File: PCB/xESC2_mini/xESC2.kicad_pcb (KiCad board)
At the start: 4 copper layers, 49.5 x 29 mm, 110 parts, among them J1 Conn_01x06_Male, J10 Conn_01x06_Male, J2 U254-051T-4BH83-F1S, J3 Conn_01x05_Male, J4 Conn_01x05_Male, J5 Conn_01x03_Male, J6 Conn_02x02_Counter_Clockwise, J7 Conn_02x02_Counter_Clockwise, J8 Conn_02x02_Counter_Clockwise, J9 Conn_01x06_Male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

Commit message: xESC mini v1.0
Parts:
- removed G***: LOGO, x-tech-logo:x-tech-logo
- removed REF**: ESD-Logo_6.6x6mm_SilkScreen, Symbol:ESD-Logo_6.6x6mm_SilkScreen
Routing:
- net /MCU/FAULT: track 38.7 -> 38.3 mm, vias 3 -> 2
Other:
- board text added: "xESC mini v1.0"
- board text removed: "CANH"
- board text removed: "CANL"
- board text removed: "CS"
- board text removed: "GND"
- board text removed: "HALL1"
- board text removed: "HALL2"
- board text removed: "HALL3"
- board text removed: "MISO"
- board text removed: "MOSI"
- board text removed: "RESET"
- board text removed: "SCK"
- board text removed: "SWDCLK"
- board text removed: "SWDIO"
- board text removed: "TEMP_MOTOR"
- board text removed: "VCC"
- board text removed: "v2.0 - License CC BY-NC-SA 4.0 https://github.com/ClemensElflein/xESC"

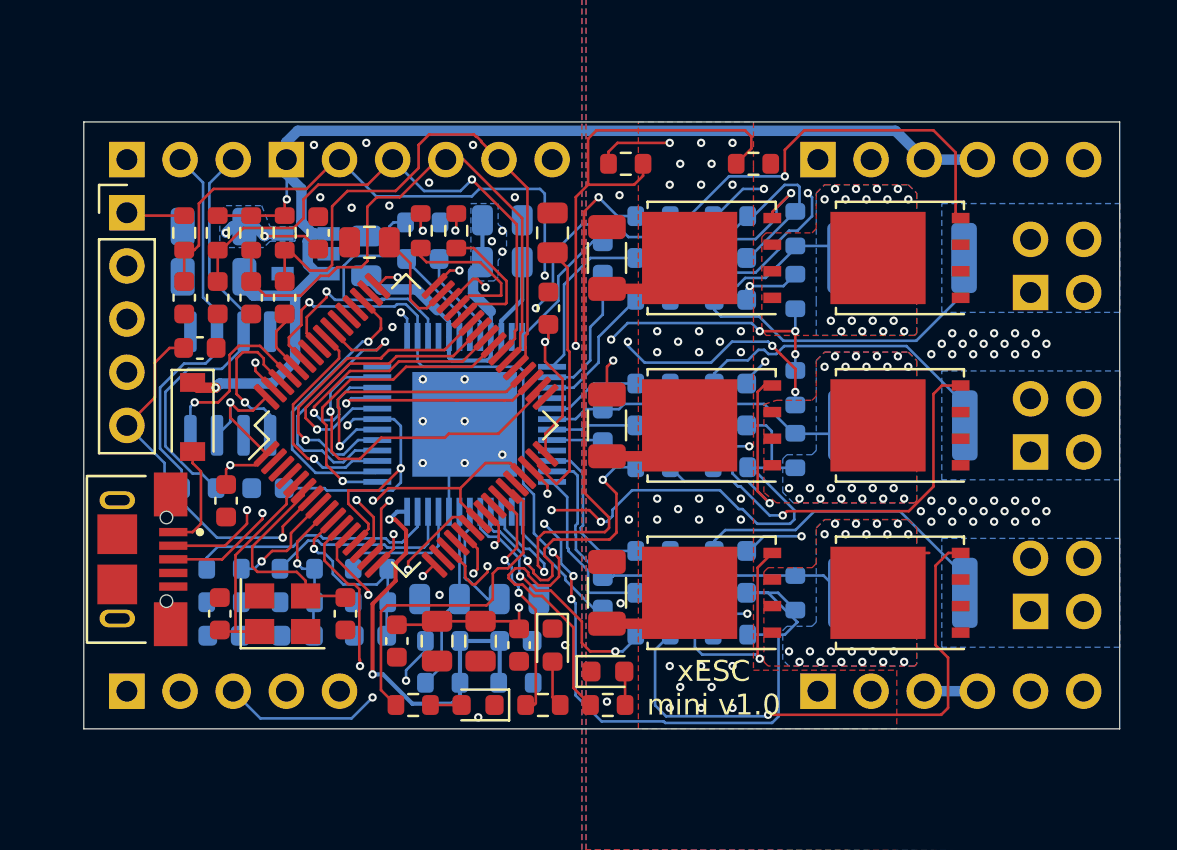
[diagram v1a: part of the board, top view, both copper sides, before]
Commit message: fixed, vias now 0.45
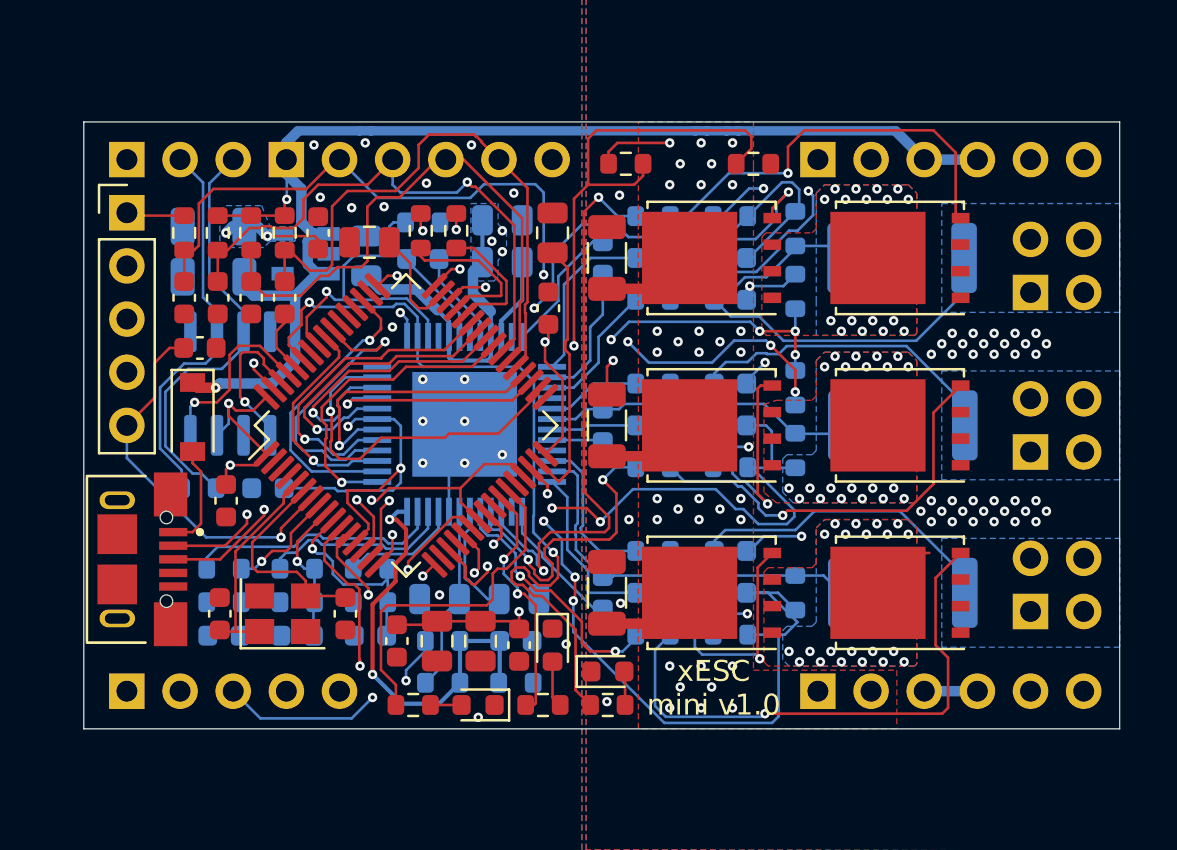
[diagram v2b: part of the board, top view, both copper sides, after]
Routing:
- net /PHASE_U_FILTERED: track 40.7 -> 39.1 mm
- net /CURU_5V: track 6.43 -> 5.67 mm
- net Net-(J2-Pad3): track 30.7 -> 30.1 mm
- net /HALL1: track 26.5 -> 27.0 mm
- net /MCU/CAN_TX: track 8.38 -> 7.88 mm
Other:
- net class Default: via_dia 0.4 -> 0.45
- rule via_min_size: 0.4 -> 0.45

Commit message: added test firmware (wip)
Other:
- board text added: "xESC mini v1.1"
- board text removed: "xESC mini v1.0"
